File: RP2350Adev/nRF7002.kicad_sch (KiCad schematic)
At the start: 8 parts, among them U1 NRF7002-QFAA-R, U4 CX1612DB40000D0WLLCC

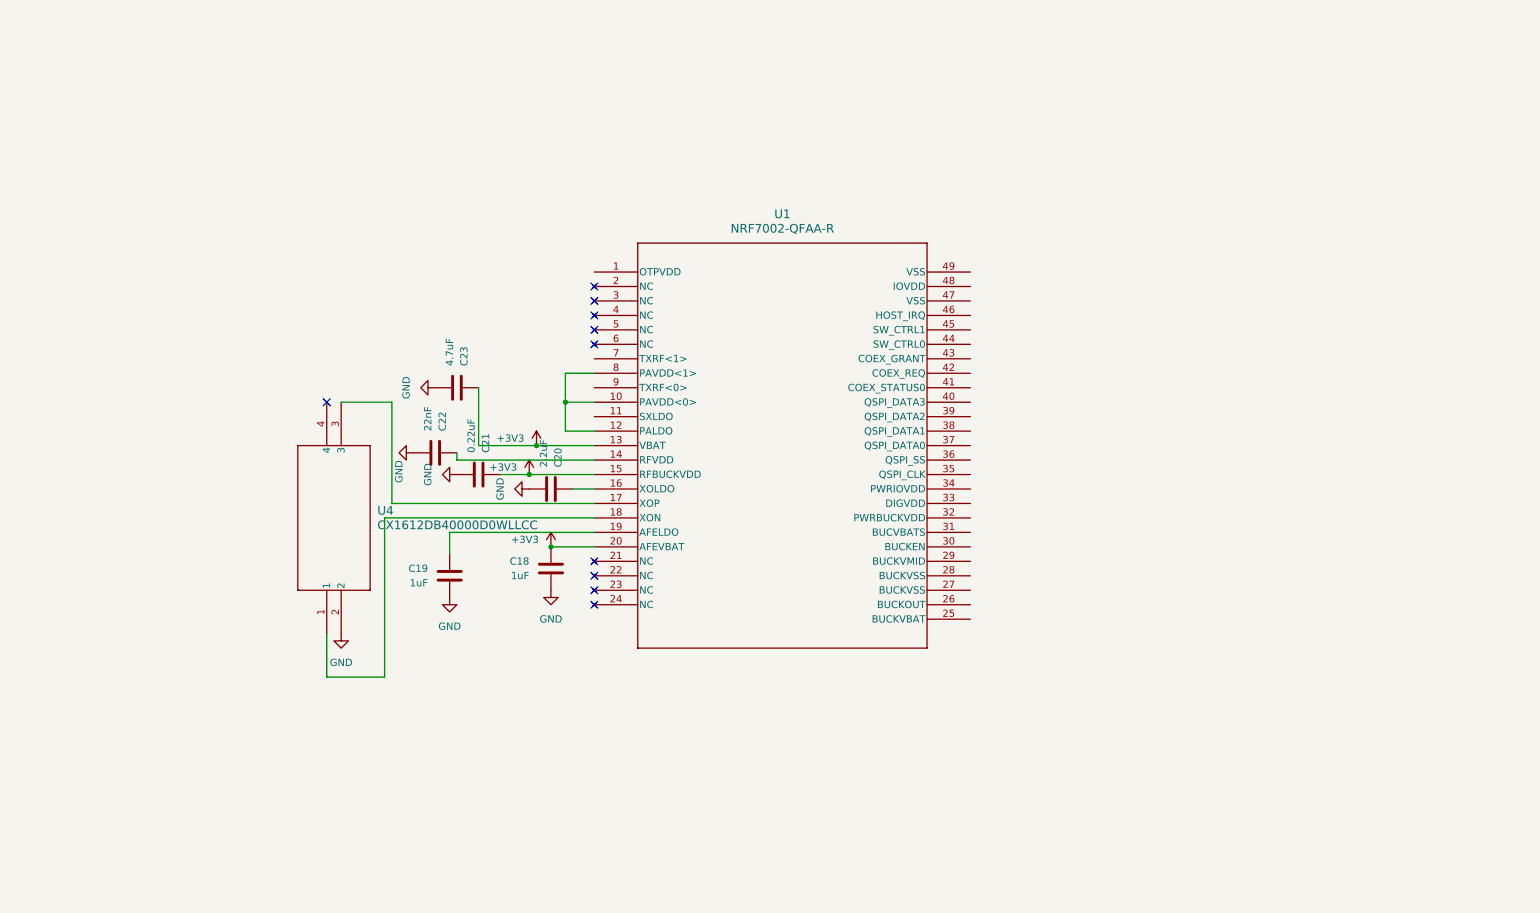
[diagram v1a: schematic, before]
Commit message: Combine subsheets
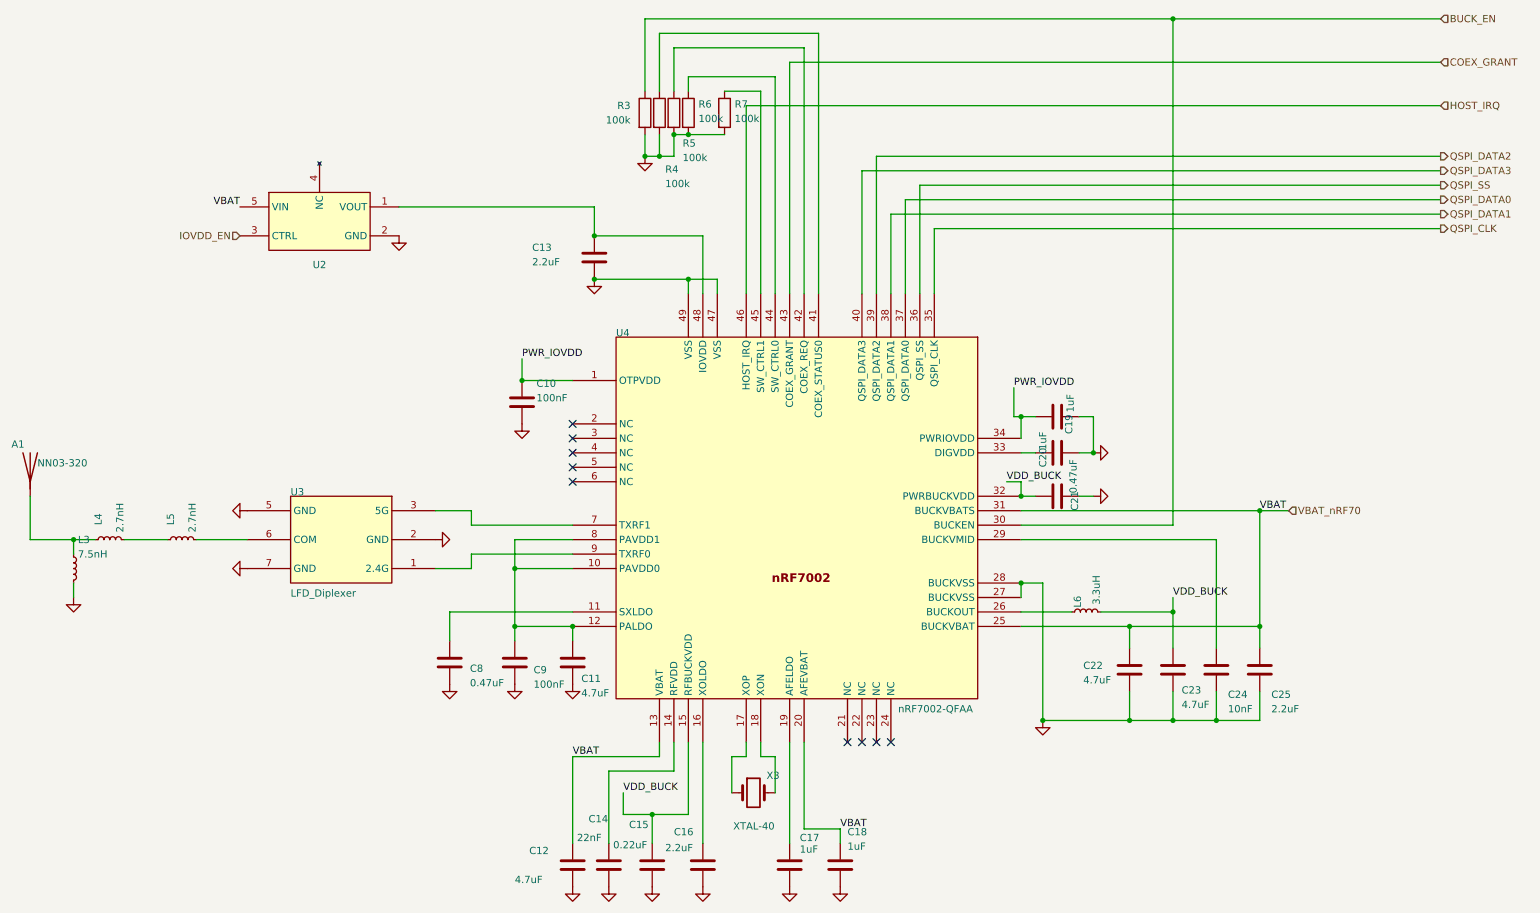
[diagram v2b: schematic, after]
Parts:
- removed U1: NRF7002-QFAA-R, QFN48_6X6_NOR, symbol 2026-04-09_15-29-49:NRF7002-QFAA-R
- removed U4: CX1612DB40000D0WLLCC, SON_CX1612DB40000D0WLLCC_KAV, symbol 2026-04-09_15-44-37:CX1612DB40000D0WLLCC
- added A1: NN03-320, Eclectronics:XCVR_NN03-320, symbol Device:Antenna
- added C10, C9: 100nF, Capacitor_SMD:C_0603_1608Metric, symbol Device:C
- added C11, C12: 4.7uF, Capacitor_SMD:C_0805_2012Metric, symbol Device:C
- added C13: 2.2uF, Capacitor_SMD:C_0805_2012Metric, symbol Device:C
- added C14: 22nF, Capacitor_SMD:C_0603_1608Metric, symbol Device:C
- added C15: 0.22uF, Capacitor_SMD:C_0603_1608Metric, symbol Device:C
- added C16, C25: 2.2uF, Capacitor_SMD:C_0603_1608Metric, symbol Device:C
- added C17: 1uF, Capacitor_SMD:C_0603_1608Metric, symbol Device:C
- added C24: 10nF, Capacitor_SMD:C_0603_1608Metric, symbol Device:C
- added C8: 0.47uF, Capacitor_SMD:C_0603_1608Metric, symbol Device:C
- added L3: 7.5nH, Inductor_SMD:L_0603_1608Metric, symbol Device:L_Small
- added L4, L5: 2.7nH, Inductor_SMD:L_0603_1608Metric, symbol Device:L_Small
- added L6: 3.3uH, Inductor_SMD:L_1008_2520Metric, symbol Device:L_Small
- added R3, R4, R5, R6, R7: 100k, Resistor_SMD:R_0402_1005Metric, symbol Device:R
- added U2: ~, Package_TO_SOT_SMD:SC-74A-5_1.55x2.9mm_P0.95mm, symbol 2026-04-09_15-29-49:TCK106AF
- added U3: LFD_Diplexer, Eclectronics:FIL_LFD182G45DCJD247, symbol 2026-04-09_15-29-49:LFD_Diplexer
- added U4: nRF7002-QFAA, Package_DFN_QFN:QFN-48-1EP_6x6mm_P0.4mm_EP4.66x4.66mm_ThermalVias, symbol 2026-04-09_15-29-49:nRF7002
- added X3: XTAL-40, Crystal:Crystal_SMD_Abracon_ABM3-2Pin_5.0x3.2mm, symbol Device:Crystal
- C18, C19: footprint Resistor_SMD:R_0402_1005Metric -> Capacitor_SMD:C_0603_1608Metric
- C20: value 2.2uF -> 1uF; footprint Resistor_SMD:R_0402_1005Metric -> Capacitor_SMD:C_0603_1608Metric
- C21: value 0.22uF -> 0.47uF; footprint Resistor_SMD:R_0402_1005Metric -> Capacitor_SMD:C_0603_1608Metric
- C22: value 22nF -> 4.7uF; footprint Resistor_SMD:R_0402_1005Metric -> Capacitor_SMD:C_0805_2012Metric
- C23: footprint Resistor_SMD:R_0402_1005Metric -> Capacitor_SMD:C_0805_2012Metric
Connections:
- net +3V3 is gone; now on net GND: C18.2, C21.2, C23.2
- net GND: now also C19.2, C20.2, C22.2, C10.2, C11.2, C12.2, C13.2, C14.2, C15.2, C16.2, C17.2, C24.2, C25.2, C8.2, C9.2, L3.2, R3.2, R4.2, R5.2, R6.2, R7.2, U2.2 (GND), U3.2 (GND), U3.5 (GND), U3.7 (GND), U4.27 (BUCKVSS), U4.28 (BUCKVSS), U4.47 (VSS), U4.49 (VSS); no longer C18.1, C19.1, C20.1, C21.1, C22.1, C23.1
- new net: A1.1 (A), L3.1, L4.1
- new net: C11.1, C9.1, U4.10 (PAVDD0), U4.12 (PALDO), U4.8 (PAVDD1)
- new net: R7.1, U4.45 (SW_CTRL1)
- new net: R4.1, U4.41 (COEX_STATUS0)
- new net: R5.1, U4.42 (COEX_REQ)
- new net: C17.1, U4.19 (AFELDO)
- new net: L6.1, U4.26 (BUCKOUT)
- new net: C13.1, U2.1 (VOUT), U4.48 (IOVDD)
- new net: R6.1, U4.44 (SW_CTRL0)
- new net: C20.1, U4.33 (DIGVDD)
- new net: C8.1, U4.11 (SXLDO)
- new net: L4.2, L5.1
- new net: C16.1, U4.16 (XOLDO)
- new net: U4.17 (XOP), X3.1
- new net: U4.18 (XON), X3.2
- new net: L5.2, U3.6 (COM)
- new net: C24.1, U4.29 (BUCKVMID)
- new net: C14.1, U4.14 (RFVDD)
- new net: U3.1 (2.4G), U4.9 (TXRF0)
- new net: U3.3 (5G), U4.7 (TXRF1)
- new net BUCK_EN: R3.1, U4.30 (BUCKEN)
- new net COEX_GRANT: U4.43 (COEX_GRANT)
- new net HOST_IRQ: U4.46 (HOST_IRQ)
- new net IOVDD_EN: U2.3 (CTRL)
- new net PWR_IOVDD: C10.1, C19.1, U4.1 (OTPVDD), U4.34 (PWRIOVDD)
- new net QSPI_CLK: U4.35 (QSPI_CLK)
- new net QSPI_DATA0: U4.37 (QSPI_DATA0)
- new net QSPI_DATA1: U4.38 (QSPI_DATA1)
- new net QSPI_DATA2: U4.39 (QSPI_DATA2)
- new net QSPI_DATA3: U4.40 (QSPI_DATA3)
- new net QSPI_SS: U4.36 (QSPI_SS)
- new net VBAT_nRF70: C12.1, C18.1, C22.1, C25.1, U2.5 (VIN), U4.13 (VBAT), U4.20 (AFEVBAT), U4.25 (BUCKVBAT), U4.31 (BUCKVBATS)
- new net VDD_BUCK: C15.1, C21.1, C23.1, L6.2, U4.15 (RFBUCKVDD), U4.32 (PWRBUCKVDD)
- no-connect marks 10 -> 9
